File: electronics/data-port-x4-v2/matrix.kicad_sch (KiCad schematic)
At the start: 16 parts, among them U10 TCA9534APWR, U7 CH446Q, U8 CH446Q, U9 TPS60400DBVR

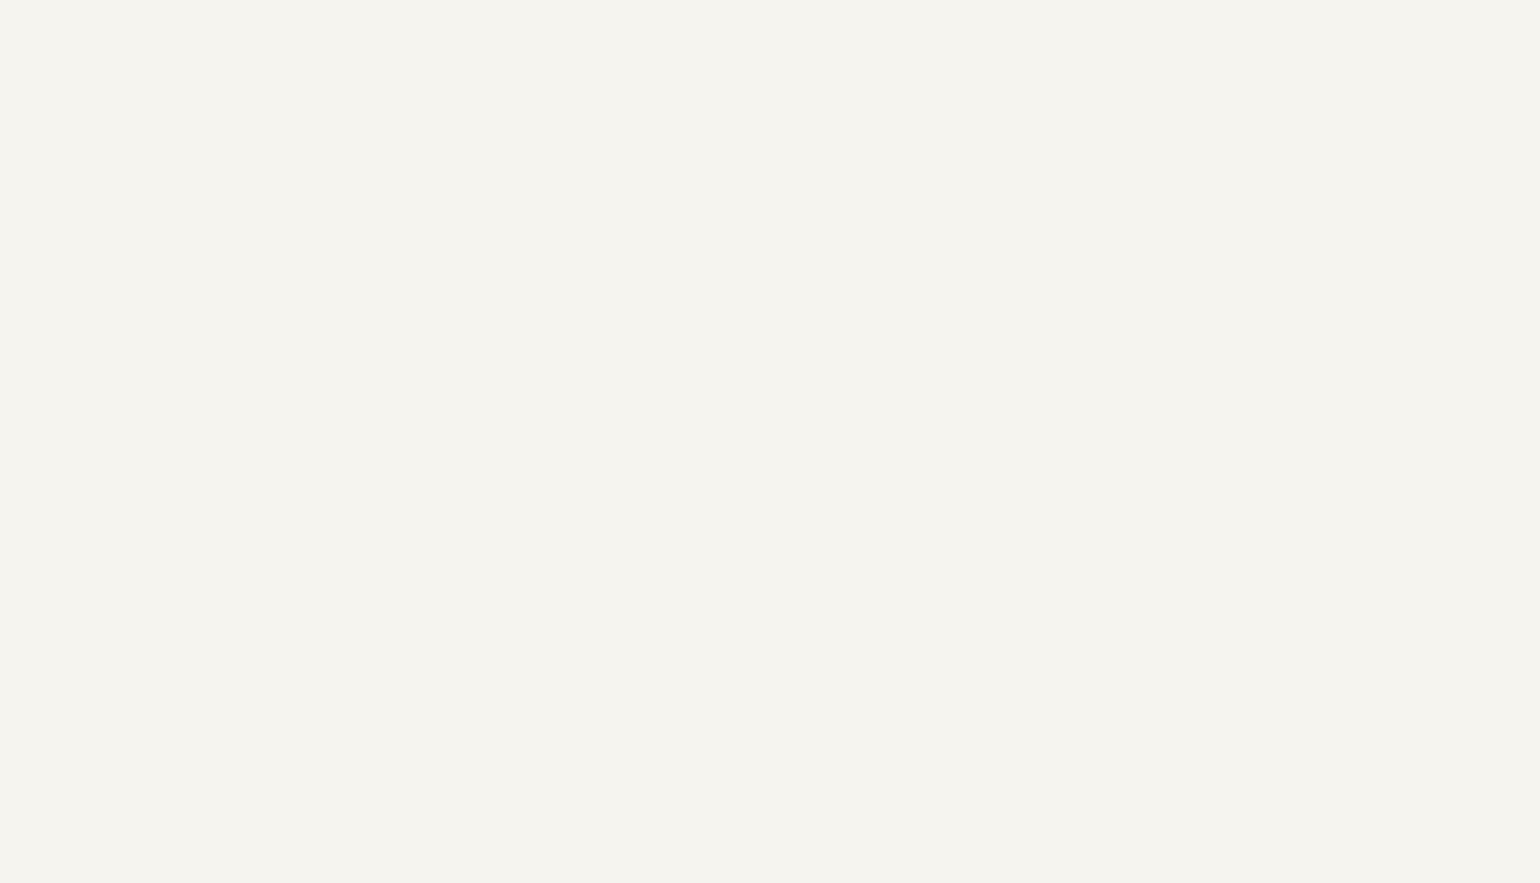
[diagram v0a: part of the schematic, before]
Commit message: DATA x4 v2: 32 labelled bring-up test points on the rear face
Eve's DFT rule on the DATA x4 v2.  Bare pads on B.Cu, mask open, no
paste, out of the BOM and the CPL (no part, no fee).  Each is named on
B.SilkS.  Supplies and GND are 1.5 mm, signals 1.0 mm (main's
"testpad1").  One table in design.py (TPS) holds every position, and
each sheet places its own.

- Co-processor row along the top edge: BOOT, RUN, SWDIO, SWCLK, GND,
  +3V3_CP.  SWD moves here from the front face.  +1V1 sits under the
  chip, on its own rear track.
- Matrix, left column: DAT, CK, STB2, GND, -5V, +5V_MX, GND; STB1 and
  MX RST on their own rear tracks.
- Supplies by the LDO: +3V3, GND, the lead's +5V.
- Hub: HUB RST, GND, 1V8.  Below J1: INT, SDA, SCL (the board side of
  the lead's isolation) and GND.
- Each port's FAULT_N (TP101-TP401) on its own rear track, and a GND by
  each pair's expander.
- Left out: VREF, RESET_N and BOOT_N (on the headers), the lead's lines
  (on J1) and the USB pairs.
- The logic's pads are marked LOGIC ONLY: the base leaves those parts
  off, so they float there.

Every pad is more than 2 mm from the THT pads and from J1, and clear of
the cradle ends, the push band and the notches.  The closest are TP23,
2.0 mm from J1's courtyard, and TP27, 2.1 mm from J101.

Routing: the old routing is seeded as protected wiring, so Freerouting
only adds the new links.  Where it gave up, the pad sits on a rear track
of its own net, or a short drawn link joins it (RUN onto CP_RUN's track,
+3V3_CP through a via to FB2).  The import's tidy pass is applied.

Checks: ERC 0, DRC 0 errors, unconnected 0, parity 0.  The 4
silk_over_copper warnings are the same on main.  Flow-through ESD check
BAD 0.  The fab outputs, panel, renders and GLBs are regenerated; the
BOM and CPL are unchanged.  docs/electronics.md lists the points, and
the "Test pads" table gains the board.

Co-Authored-By: Claude Opus 5.5 <noreply@anthropic.com>
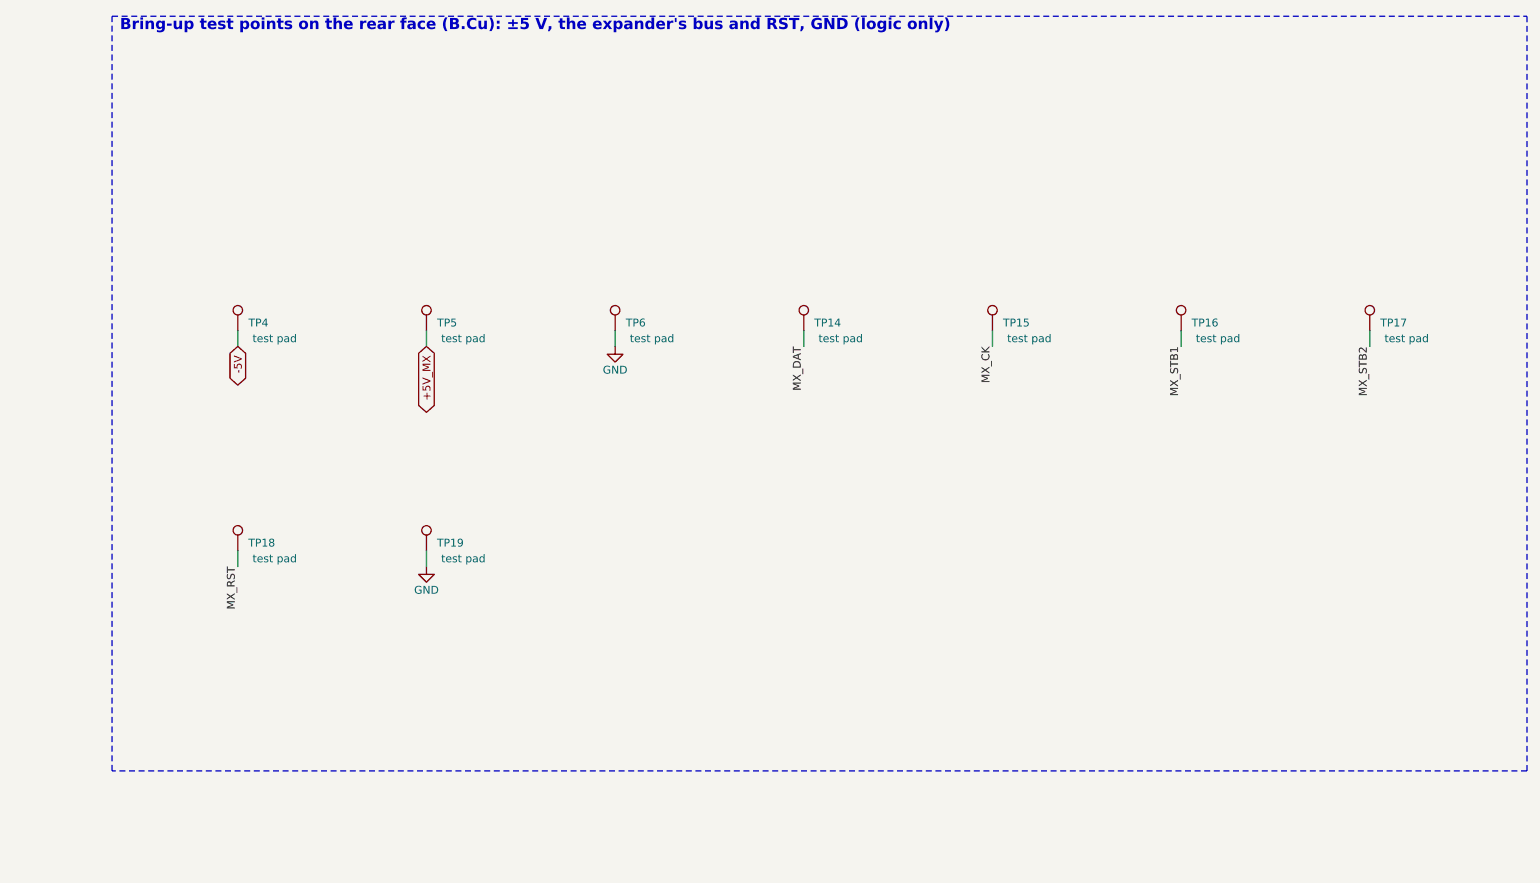
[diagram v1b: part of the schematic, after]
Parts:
- added TP14, TP15, TP16, TP17, TP18: test pad, TestPoint:TestPoint_Pad_D1.0mm, symbol Connector:TestPoint
- added TP19, TP4, TP5, TP6: test pad, TestPoint:TestPoint_Pad_D1.5mm, symbol Connector:TestPoint
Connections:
- net +5V_MX: now also TP5.1
- net -5V: now also TP4.1
- net GND: now also TP19.1, TP6.1
- net MX_CK: now also TP15.1
- net MX_DAT: now also TP14.1
- net MX_RST: now also TP18.1
- net MX_STB1: now also TP16.1
- net MX_STB2: now also TP17.1
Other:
- note added: "Bring-up test points on the rear face (B.Cu): ±5 V, the expander's bus and RST, GND (logic only)"

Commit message: DATA x4 v2: rear test pads on buses A-H and the expanders' RESET
Eve's DFT review asked for probe points on the eight crosspoint buses
and on both TCA6408A RESET lines, with a GND beside them.  Eleven bare
rear pads (TPS, out of the BOM and CPL, named on B.SilkS):

- TP29-TP36, buses A to H (1.0 mm), behind the co-processor's east
  side where all eight pass.  A, B, E and F sit on a rear track of their
  own, C, D and G beside one; H, front only, comes down a drawn via.
  Each goes where its bus passes, 2.6 mm or more from the next.
- TP37 GND (1.5 mm), with a drawn via east of it: the automatic one
  went west and moved RN8's +3V3 dog-bones.
- TP38 / TP39 EXP1 / EXP2 RST, each by its pull-up's via.

Every pad is 3.4 mm or more from a THT pad or J1.  The bus group
carries a LOGIC ONLY mark.  The router re-ran only for the new links:
BUS_H's front track moved 0.2 mm onto the new via, and two GND
dog-bones beside it turned.

Co-Authored-By: Claude Opus 5.5 <noreply@anthropic.com>
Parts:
- added TP29, TP30, TP31, TP32, TP33, TP34, TP35, TP36: test pad, TestPoint:TestPoint_Pad_D1.0mm, symbol Connector:TestPoint
- added TP37: test pad, TestPoint:TestPoint_Pad_D1.5mm, symbol Connector:TestPoint
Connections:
- net BUS_A: now also TP29.1
- net BUS_B: now also TP30.1
- net BUS_C: now also TP31.1
- net BUS_D: now also TP32.1
- net BUS_E: now also TP33.1
- net BUS_F: now also TP34.1
- net BUS_G: now also TP35.1
- net BUS_H: now also TP36.1
- net GND: now also TP37.1
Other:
- note added: "Bring-up test points on the rear face (B.Cu): ±5 V, the expander's bus and RST, buses A–H, GND (logic only)"
- note removed: "Bring-up test points on the rear face (B.Cu): ±5 V, the expander's bus and RST, GND (logic only)"
